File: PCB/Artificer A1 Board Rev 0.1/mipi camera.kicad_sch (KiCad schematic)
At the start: 8 parts

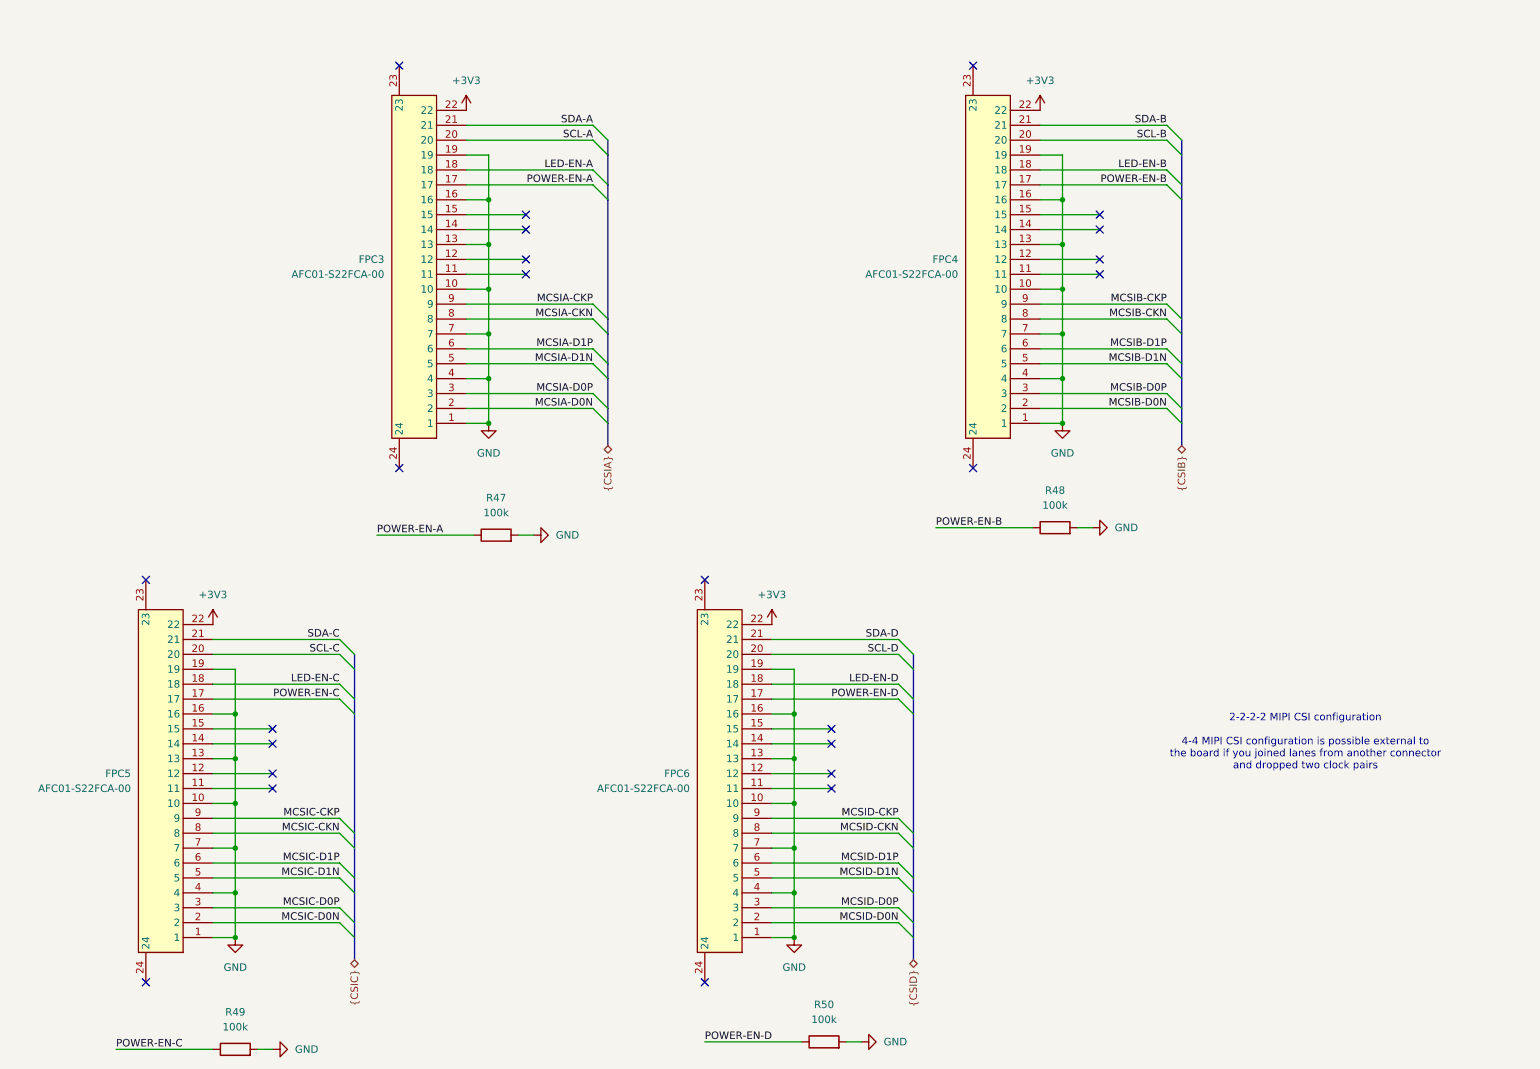
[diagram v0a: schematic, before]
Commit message: cleaned up, kicad 10 & usb c pd
migrated to Kicad 10,
added USB PD for power input
added capacitors inductors and resistor footprints
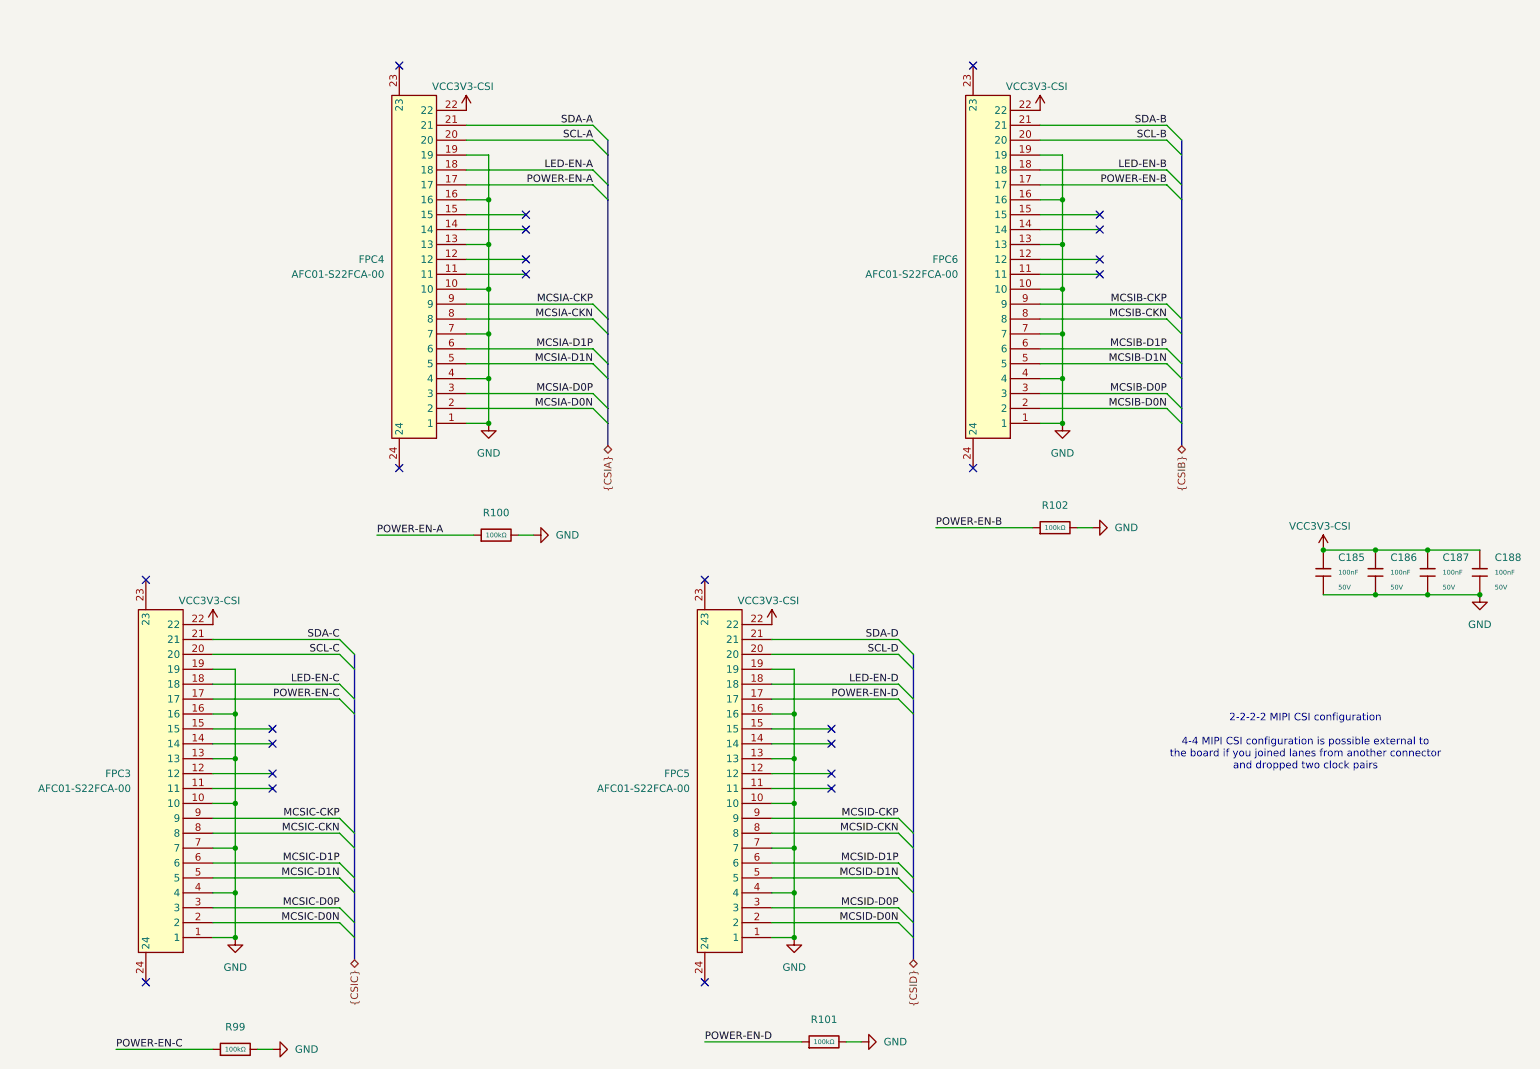
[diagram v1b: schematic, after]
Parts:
- removed R47, R48, R49, R50: 100k, symbol Device:R
- added C185, C186, C187, C188: 100nF, PCM_JLCPCB:C_0402, symbol PCM_JLCPCB-Capacitors:0402,100nF,(2)
- added R100, R101, R102, R99: 100kΩ, PCM_JLCPCB:R_0402, symbol PCM_JLCPCB-Resistors:0402,100kΩ
- renumbered FPC5 to FPC3, FPC3 to FPC4, FPC6 to FPC5, FPC4 to FPC6
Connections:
- net GND: now also C185.2, C186.2, C187.2, C188.2, R100.2, R101.2, R102.2, R99.2
- net POWER-EN-A: now also R100.1
- net POWER-EN-B: now also R102.1
- net POWER-EN-C: now also R99.1
- net POWER-EN-D: now also R101.1
- net +3V3 renamed VCC3V3-CSI
- net VCC3V3-CSI: now also C185.1, C186.1, C187.1, C188.1

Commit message: placed all components
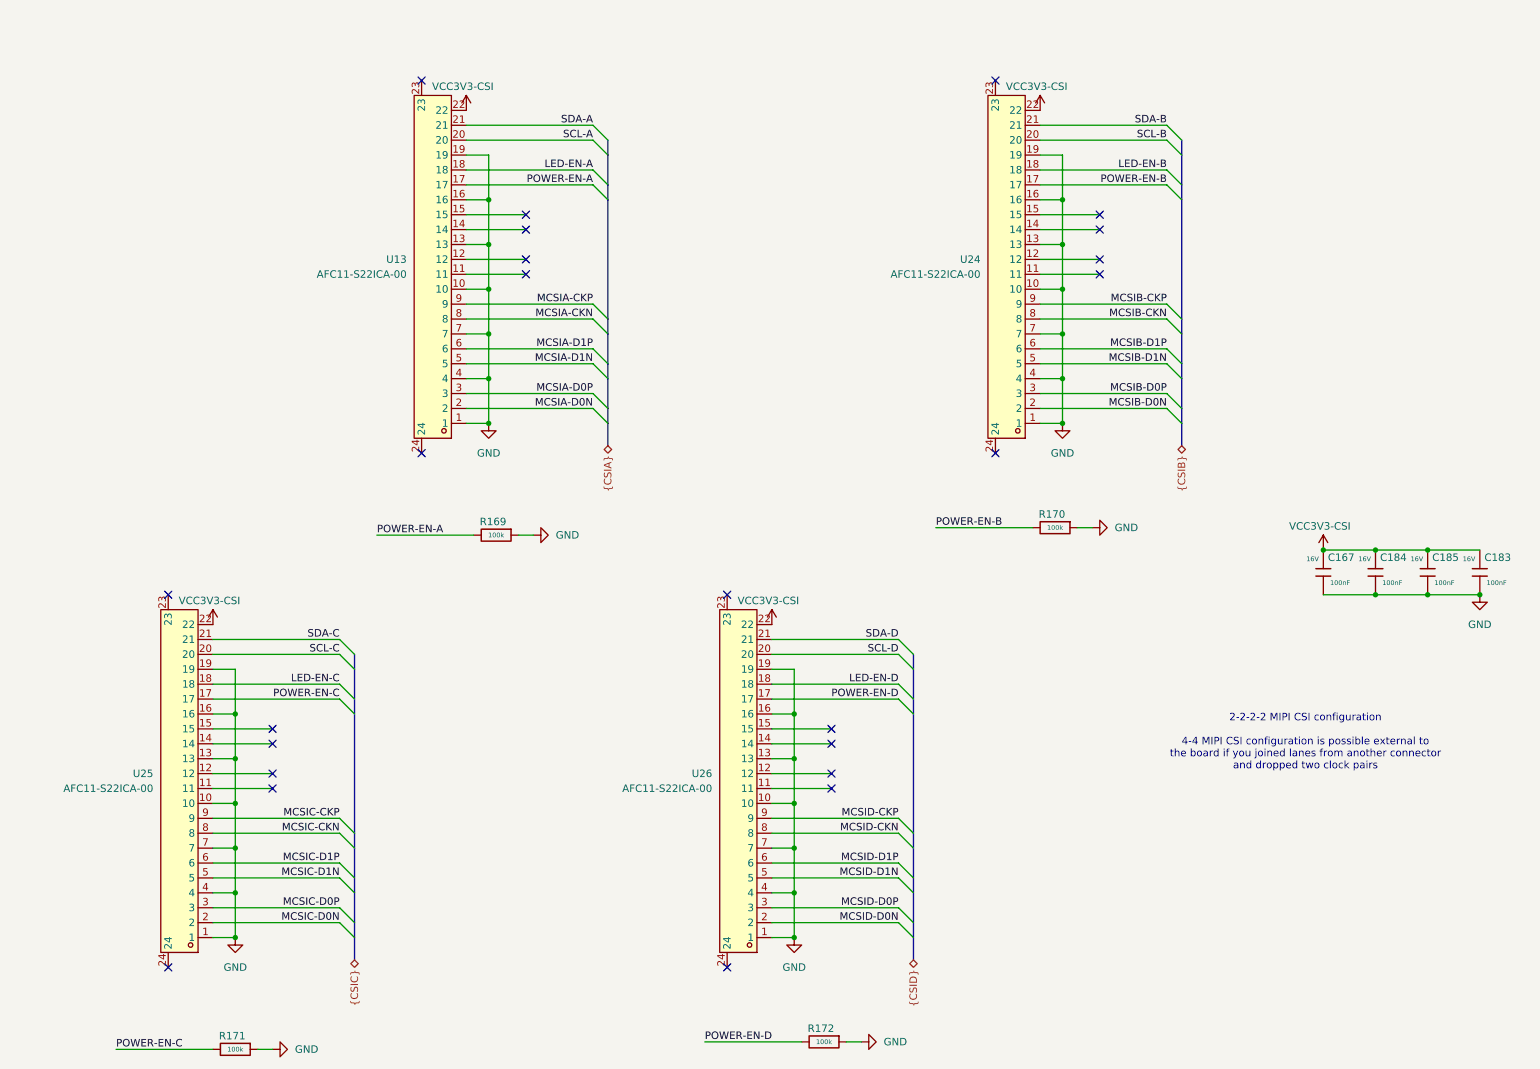
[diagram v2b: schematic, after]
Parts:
- removed C185, C186, C187, C188: 100nF, PCM_JLCPCB:C_0402, symbol PCM_JLCPCB-Capacitors:0402,100nF,(2)
- removed FPC3, FPC4, FPC5, FPC6: AFC01-S22FCA-00, easyeda:FPC-SMD_P0.5-22P_FGS-XJ-H2.0, symbol easyeda:AFC01-S22FCA-00
- removed R100, R101, R102, R99: 100kΩ, PCM_JLCPCB:R_0402, symbol PCM_JLCPCB-Resistors:0402,100kΩ
- added C167, C183, C184, C185: 100nF, Capacitor_SMD:C_0201_0603Metric, symbol Cap:JLCPCB_Lib_Blank_Cap
- added R169, R170, R171, R172: 100k, Resistor_SMD:R_0201_0603Metric, symbol Cap:JLCPCB_Res_Custom
- added U13, U24, U25, U26: AFC11-S22ICA-00, easyeda:FPC-SMD_22P-P1.00_AFC11-S22ICC-00, symbol easyeda:AFC11-S22ICA-00
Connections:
- net GND: now also C167.1, C183.1, C184.1, C185.1, R169.1, R170.1, R171.1, R172.1, U13.1, U13.10, U13.13, U13.16, U13.19, U13.4, U13.7, U24.1, U24.10, U24.13, U24.16, U24.19, U24.4, U24.7, U25.1, U25.10, U25.13, U25.16, U25.19, U25.4, U25.7, U26.1, U26.10, U26.13, U26.16, U26.19, U26.4, U26.7
- net LED-EN-A: now also U13.18
- net LED-EN-B: now also U24.18
- net LED-EN-C: now also U25.18
- net LED-EN-D: now also U26.18
- net MCSIA-CKN: now also U13.8
- net MCSIA-CKP: now also U13.9
- net MCSIA-D0N: now also U13.2
- net MCSIA-D0P: now also U13.3
- net MCSIA-D1N: now also U13.5
- net MCSIA-D1P: now also U13.6
- net MCSIB-CKN: now also U24.8
- net MCSIB-CKP: now also U24.9
- net MCSIB-D0N: now also U24.2
- net MCSIB-D0P: now also U24.3
- net MCSIB-D1N: now also U24.5
- net MCSIB-D1P: now also U24.6
- net MCSIC-CKN: now also U25.8
- net MCSIC-CKP: now also U25.9
- net MCSIC-D0N: now also U25.2
- net MCSIC-D0P: now also U25.3
- net MCSIC-D1N: now also U25.5
- net MCSIC-D1P: now also U25.6
- net MCSID-CKN: now also U26.8
- net MCSID-CKP: now also U26.9
- net MCSID-D0N: now also U26.2
- net MCSID-D0P: now also U26.3
- net MCSID-D1N: now also U26.5
- net MCSID-D1P: now also U26.6
- net POWER-EN-A: now also R169.2, U13.17
- net POWER-EN-B: now also R170.2, U24.17
- net POWER-EN-C: now also R171.2, U25.17
- net POWER-EN-D: now also R172.2, U26.17
- net SCL-A: now also U13.20
- net SCL-B: now also U24.20
- net SCL-C: now also U25.20
- net SCL-D: now also U26.20
- net SDA-A: now also U13.21
- net SDA-B: now also U24.21
- net SDA-C: now also U25.21
- net SDA-D: now also U26.21
- net VCC3V3-CSI: now also C167.2, C183.2, C184.2, C185.2, U13.22, U24.22, U25.22, U26.22

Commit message: more routing and decoupling
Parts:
- added R215, R216, R217, R218, R219, R220, R221, R222: 4.7k, Resistor_SMD:R_0201_0603Metric, symbol Cap:JLCPCB_Res_Custom
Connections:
- net SCL-A: now also R216.2
- net SCL-B: now also R218.2
- net SCL-C: now also R220.2
- net SCL-D: now also R222.2
- net SDA-A: now also R215.2
- net SDA-B: now also R217.2
- net SDA-C: now also R219.2
- net SDA-D: now also R221.2
- net VCC3V3-CSI: now also R215.1, R216.1, R217.1, R218.1, R219.1, R220.1, R221.1, R222.1
